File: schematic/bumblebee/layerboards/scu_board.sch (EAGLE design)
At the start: 24 parts

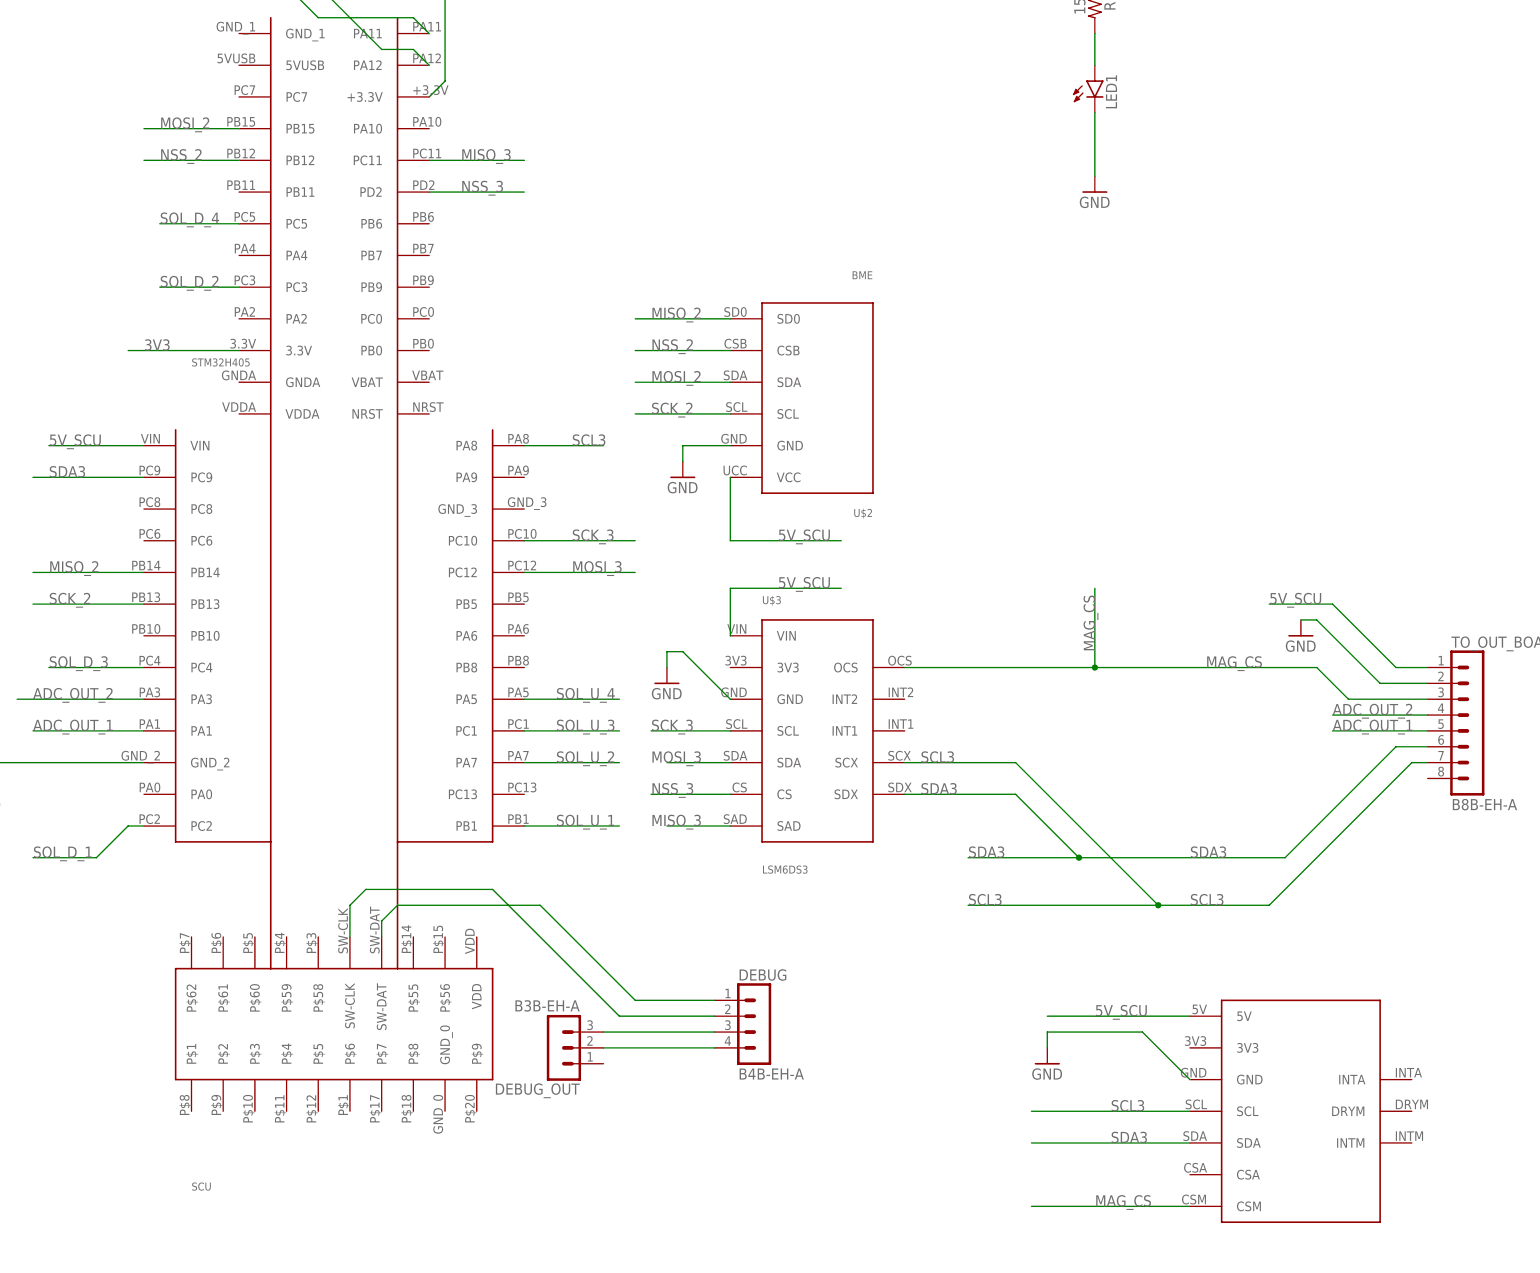
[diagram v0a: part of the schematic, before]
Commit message: Исправил библиотеку Осталось исправить внешнюю плату и сделать плату под антенну GPS
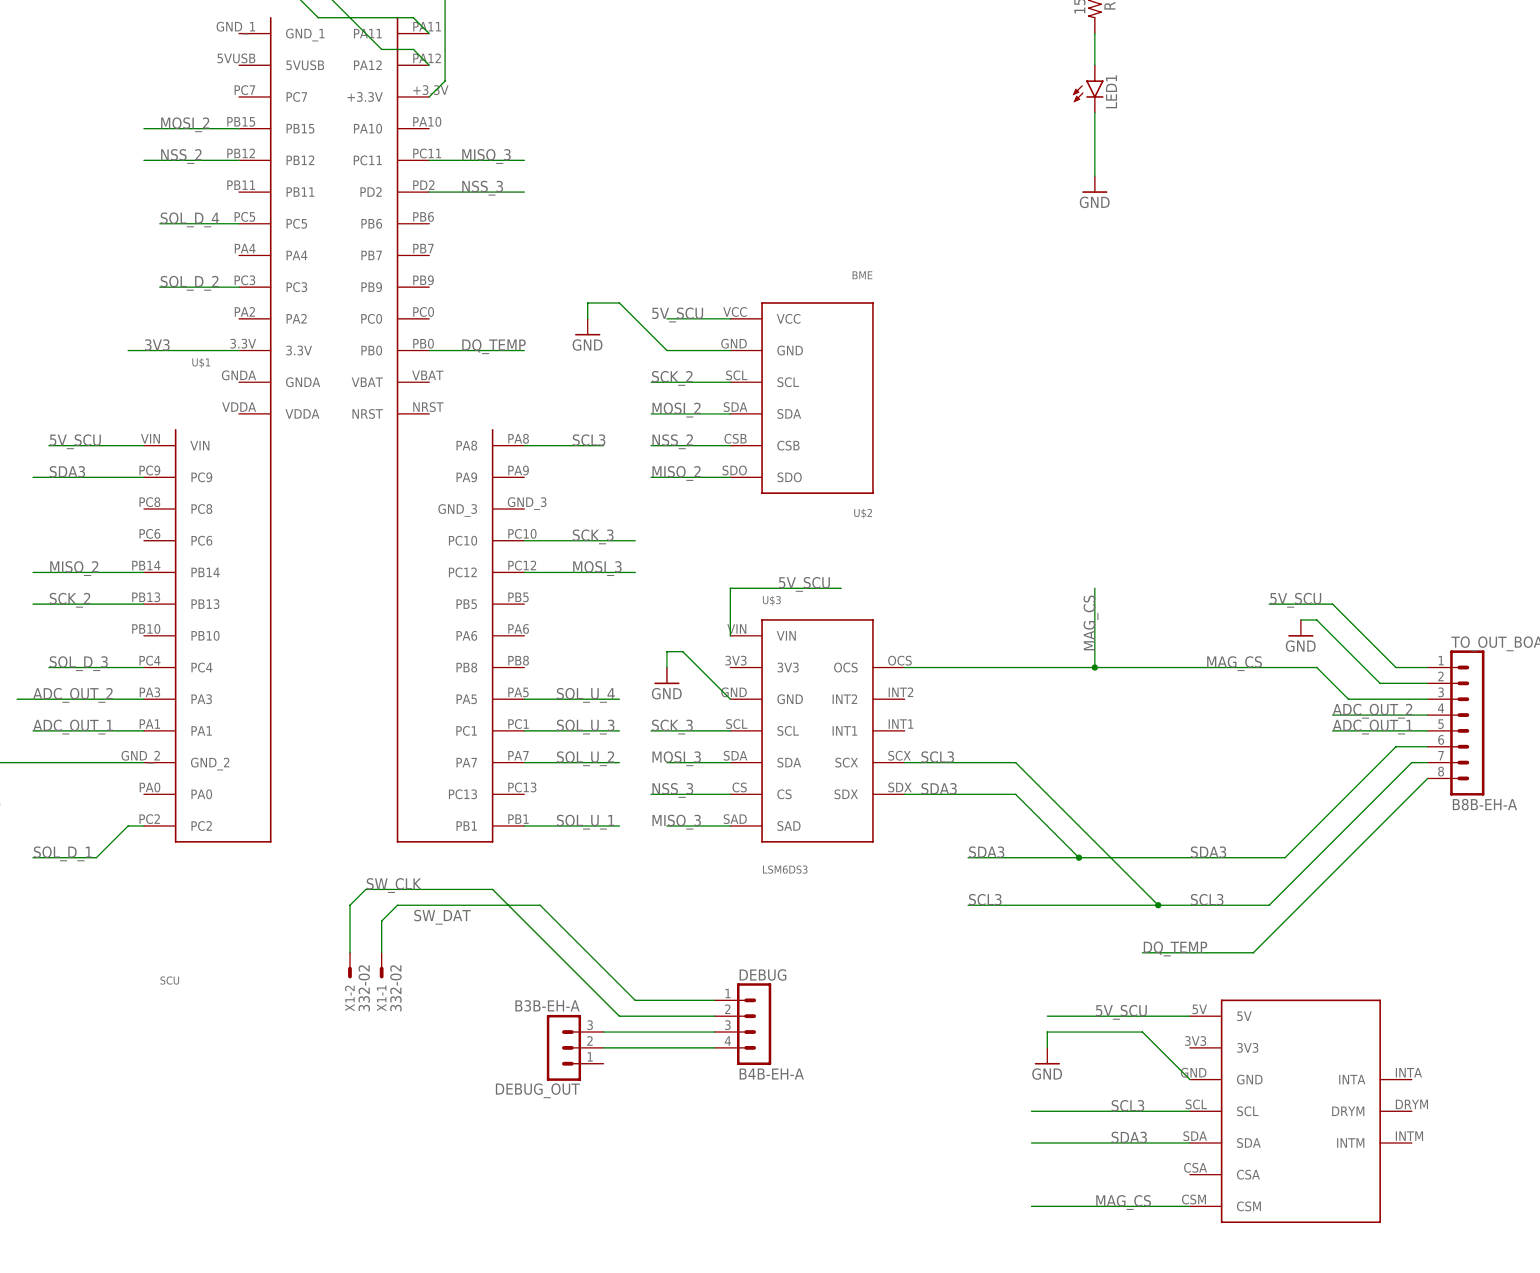
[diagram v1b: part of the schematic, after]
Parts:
- removed STM32H405: SCU, bluepill:SCU
- added U$1: SCU, bluepill:SCU
- added X1: 332-02, con-garry:332-02
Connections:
- removed net N$22: DEBUG.1, STM32H405.SW-DAT
- removed net N$24: DEBUG.2, STM32H405.SW-CLK
- new net DQ_TEMP: TO_OUT_BOARD.8, U$1.PB0
- new net SW_CLK: DEBUG.2, X1-2.S
- new net SW_DAT: DEBUG.1, X1-1.S
- net 3V3: now also U$1.3.3V; no longer STM32H405.3.3V
- net 5V_SCU: now also U$1.VIN; no longer STM32H405.VIN
- net ADC_OUT_1: now also U$1.PA1; no longer STM32H405.PA1
- net ADC_OUT_2: now also U$1.PA3; no longer STM32H405.PA3
- net GND: now also U$1.GND_2; no longer STM32H405.GND_2
- net MISO_2: now also U$1.PB14, U$2.SDO; no longer STM32H405.PB14, U$2.SD0
- net MISO_3: now also U$1.PC11; no longer STM32H405.PC11
- net MOSI_2: now also U$1.PB15; no longer STM32H405.PB15
- net MOSI_3: now also U$1.PC12; no longer STM32H405.PC12
- net N$16: now also U$1.+3.3V; no longer STM32H405.+3.3V
- net N$6: now also U$1.PA11; no longer STM32H405.PA11
- net N$7: now also U$1.PA12; no longer STM32H405.PA12
- net NSS_2: now also U$1.PB12; no longer STM32H405.PB12
- net NSS_3: now also U$1.PD2; no longer STM32H405.PD2
- net SCK_2: now also U$1.PB13; no longer STM32H405.PB13
- net SCK_3: now also U$1.PC10; no longer STM32H405.PC10
- net SCL3: now also U$1.PA8; no longer STM32H405.PA8
- net SDA3: now also U$1.PC9; no longer STM32H405.PC9
- net SOL_D_1: now also U$1.PC2; no longer STM32H405.PC2
- net SOL_D_2: now also U$1.PC3; no longer STM32H405.PC3
- net SOL_D_3: now also U$1.PC4; no longer STM32H405.PC4
- net SOL_D_4: now also U$1.PC5; no longer STM32H405.PC5
- net SOL_U_1: now also U$1.PB1; no longer STM32H405.PB1
- net SOL_U_2: now also U$1.PA7; no longer STM32H405.PA7
- net SOL_U_3: now also U$1.PC1; no longer STM32H405.PC1
- net SOL_U_4: now also U$1.PA5; no longer STM32H405.PA5
